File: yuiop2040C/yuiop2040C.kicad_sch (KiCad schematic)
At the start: 31 parts, among them J1 Conn_01x20, J2 Conn_01x20, J3 Conn_01x03, U1 RP2040, U2 W25Q16JVSS, U3 MIC5219-3.3YM5, Y1 FA238V 12.000000MHz 10.0 +50.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

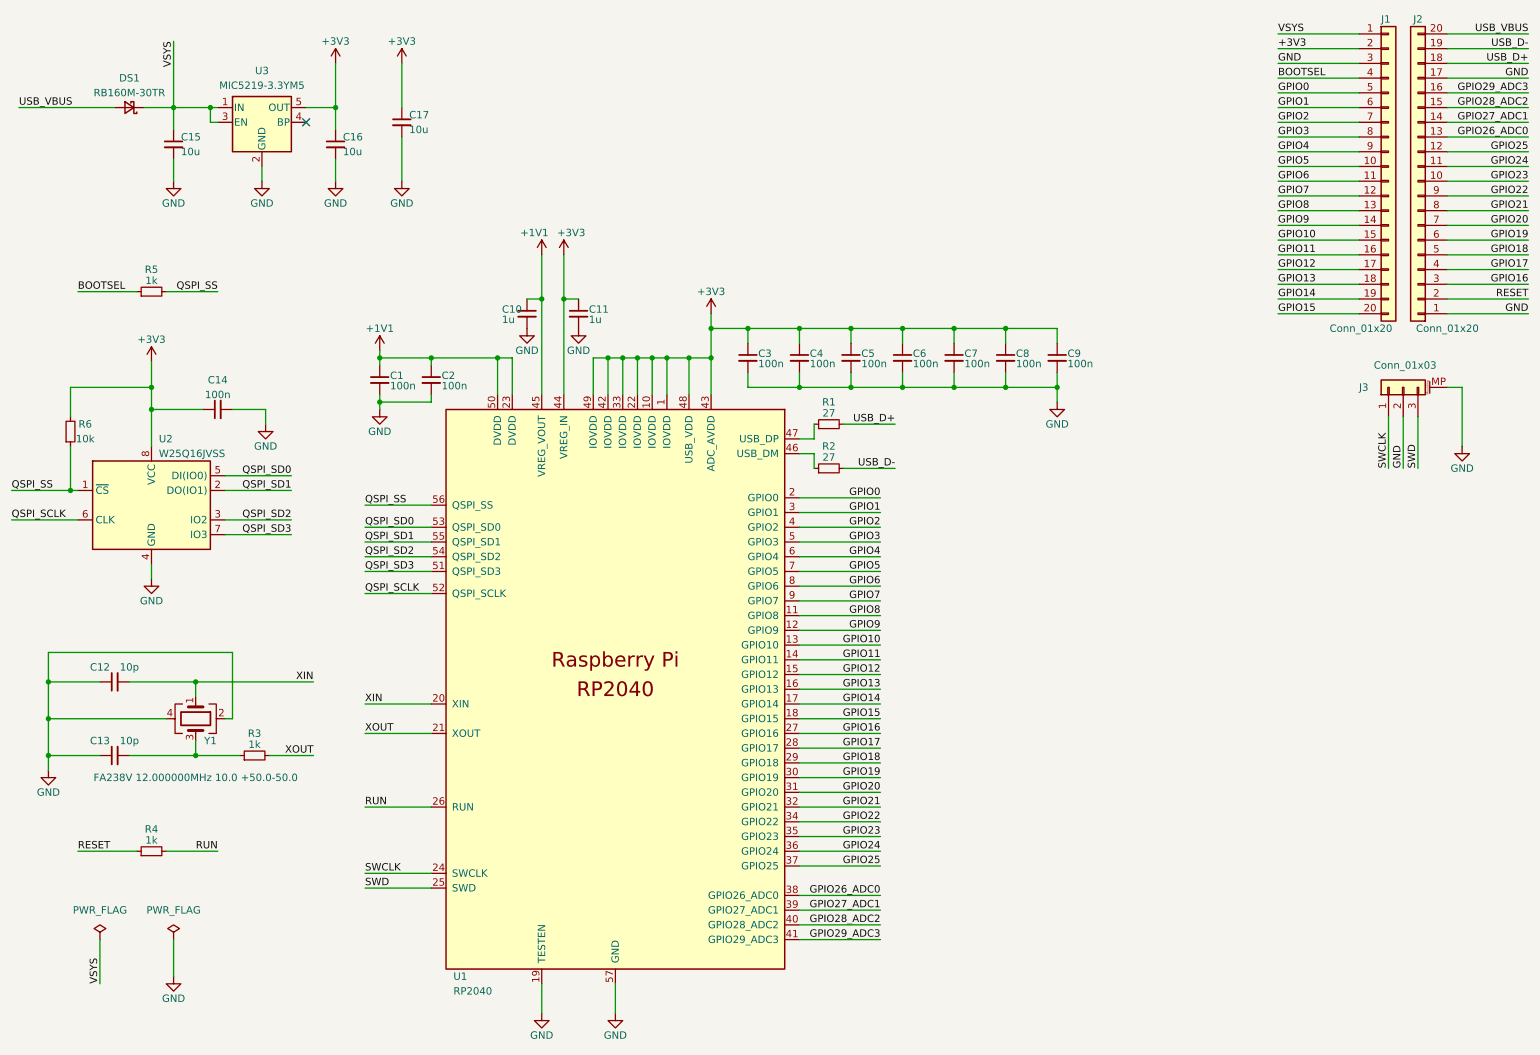
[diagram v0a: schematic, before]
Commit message: KiCad 8: convert yuiop2040C
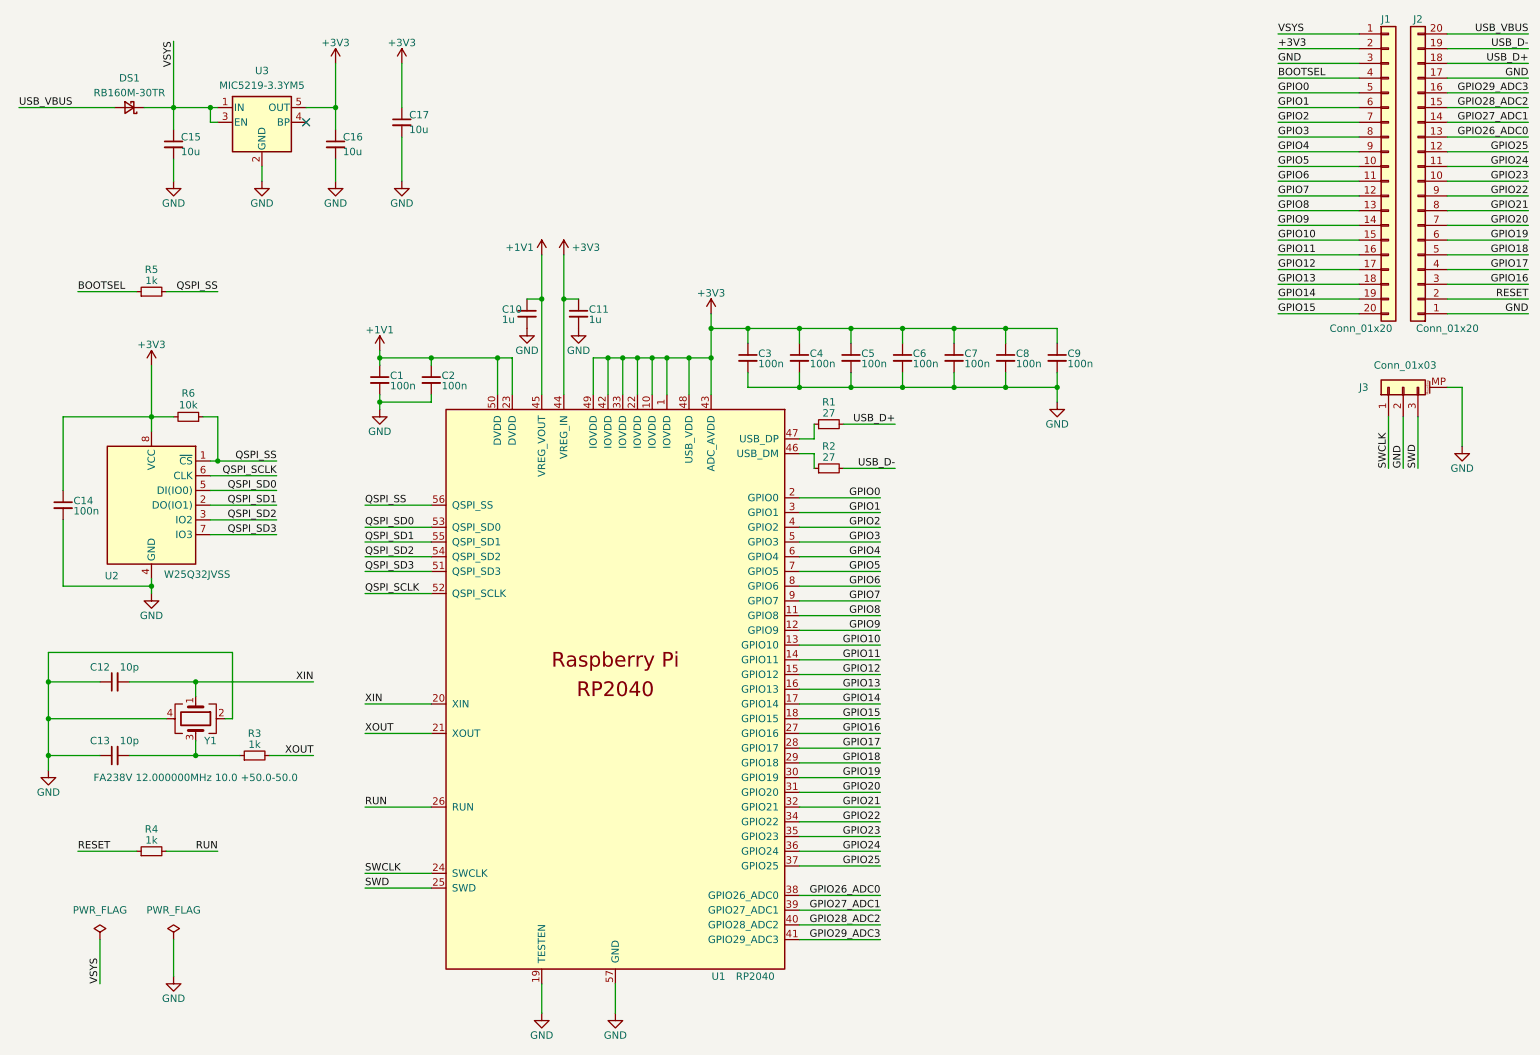
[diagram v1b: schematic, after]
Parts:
- U2: value W25Q16JVSS -> W25Q32JVSS
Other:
- moved on the sheet: R6, U2
